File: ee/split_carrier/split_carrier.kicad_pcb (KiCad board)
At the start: 2 copper layers, 127 x 101.6 mm, 11 parts, among them J1 Conn_01x08, J2 Conn_01x08, J3 Conn_01x08, J4 Conn_01x08, J5 Conn_01x04, J6 STM32F0_Discovery_Header, U2 RC1602A

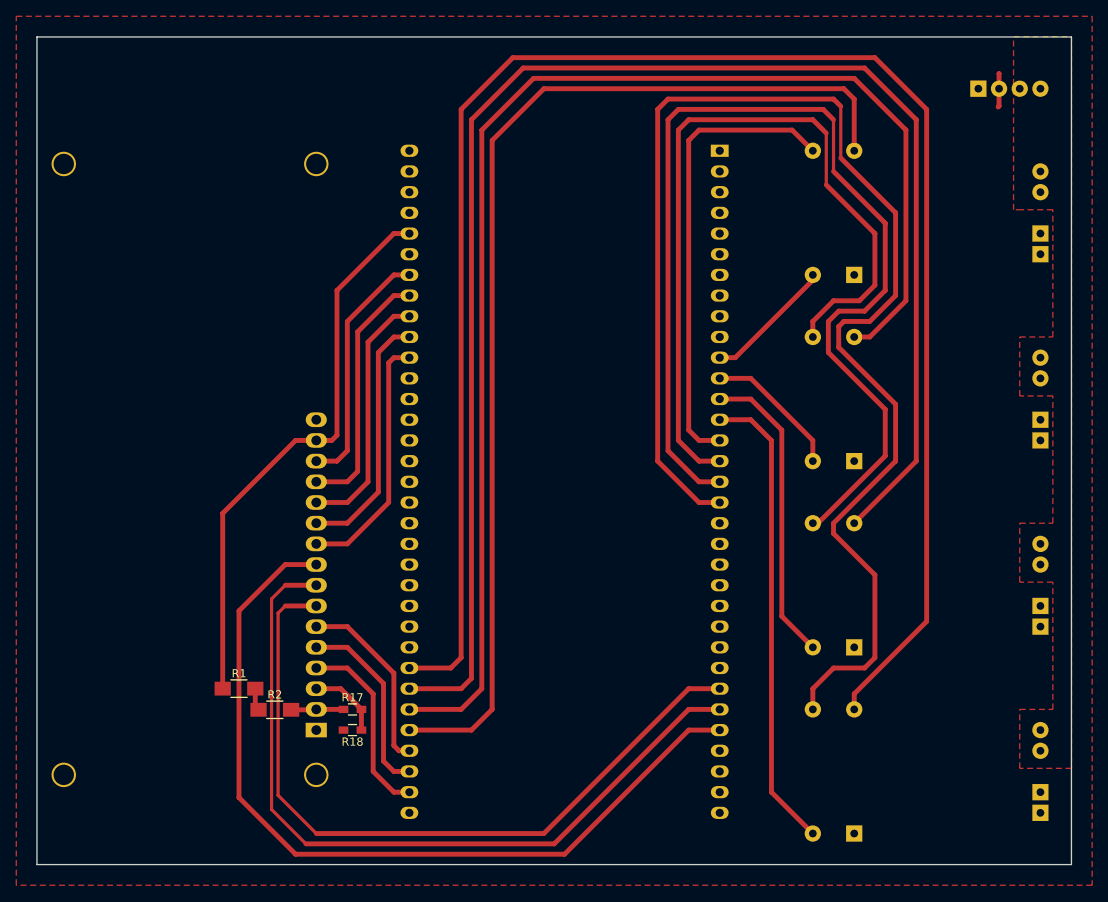
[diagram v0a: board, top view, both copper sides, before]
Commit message: update layout for carrier with new pin assignments
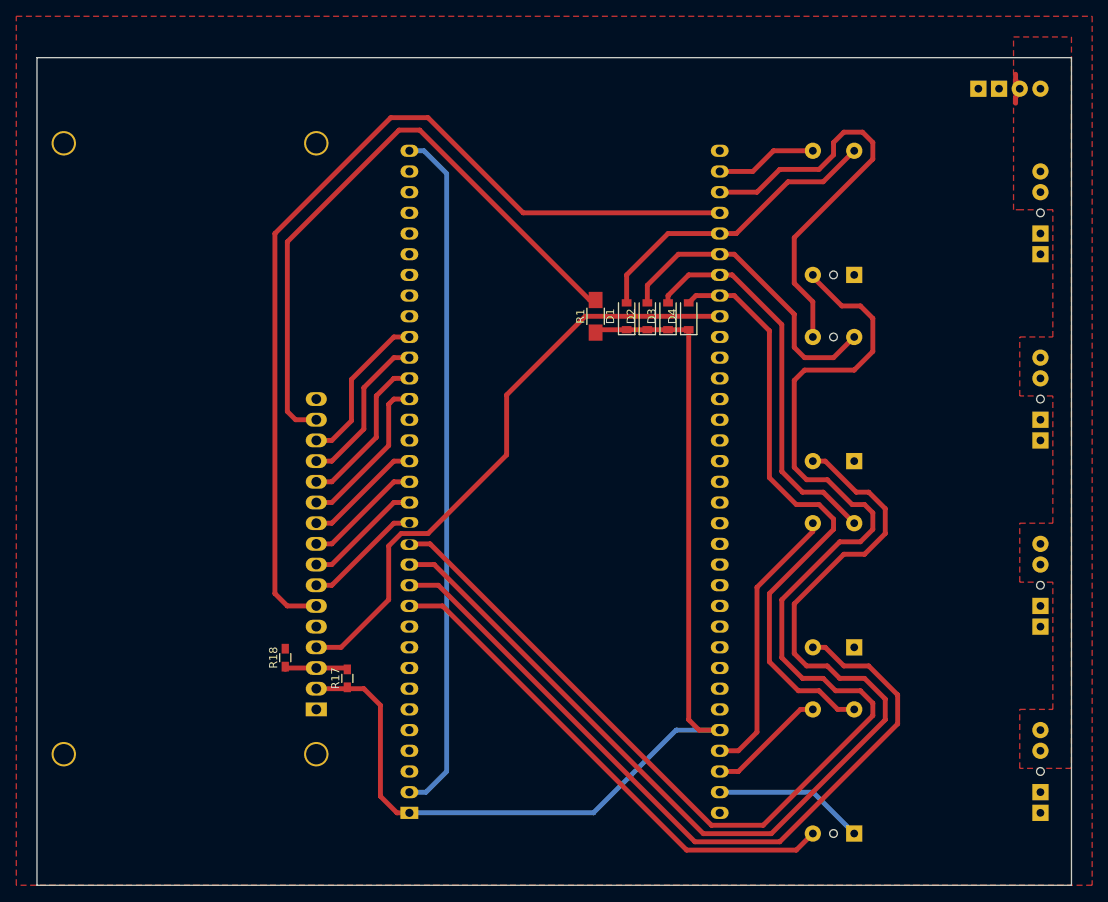
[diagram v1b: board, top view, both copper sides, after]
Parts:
- removed R2: 0, Resistors_SMD:R_1206_HandSoldering
- added D1: D_Schottky, Diodes_SMD:D_SOD-123, F.Cu at (72.4, 34.3)
- added D2: D_Schottky, Diodes_SMD:D_SOD-123, F.Cu at (74.9, 34.3)
- added D3: D_Schottky, Diodes_SMD:D_SOD-123, F.Cu at (77.5, 34.3)
- added D4: D_Schottky, Diodes_SMD:D_SOD-123, F.Cu at (80.0, 34.3)
- J1, J2, J3, J4: footprint custom:Fan_Controller -> custom:Fan_Controller_all
- moved R1 63.3 mm to (68.6, 34.3), turned to 90 degrees
- moved R18 12.1 mm to (30.5, 76.2), turned to 90 degrees
- moved R17 3.86 mm to (38.1, 78.7), turned to 90 degrees
- moved U2 2.54 mm to (34.3, 82.5)
- turned J6 to 270 degrees
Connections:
- net Net-(J6-Pad25) renamed /FAN4_ADC
- net Net-(J6-Pad26) renamed /FAN5_ADC
- net Net-(J6-Pad30) renamed /FAN6_CTRL
- net Net-(J6-Pad31) renamed /FAN7_CTRL
- net Net-(J6-Pad43) renamed /UART1_TX
- net Net-(J6-Pad44) renamed /UART1_RX
- net Net-(J6-Pad47) renamed /SWDIO
- net Net-(J6-Pad50) renamed /SWCLK
- net Net-(J6-Pad51) renamed /FAN4_CTRL
- J6 pad 1: Net-(J6-Pad1) -> +3V3
- J6 pad 11: /FAN0_ADC -> /FAN3_ADC
- J6 pad 12: /FAN1_ADC -> /FAN2_ADC
- J6 pad 13: /FAN2_ADC -> /FAN1_ADC
- J6 pad 14: /FAN3_ADC -> /FAN0_ADC
- J6 pad 15: /FAN0_RPM -> /LCD_D0
- J6 pad 16: /FAN1_RPM -> /LCD_D1
- J6 pad 17: /FAN2_RPM -> /LCD_D2
- J6 pad 18: /FAN3_RPM -> /LCD_D3
- J6 pad 21: Net-(J6-Pad21) -> /LCD_D4
- J6 pad 22: Net-(J6-Pad22) -> /LCD_D5
- J6 pad 23: Net-(J6-Pad23) -> /LCD_D6
- J6 pad 24: Net-(J6-Pad24) -> /LCD_D7
- J6 pad 27: /LCD_D0 -> /FAN6_ADC
- J6 pad 28: /LCD_D1 -> /FAN7_ADC
- J6 pad 29: /LCD_D2 -> Net-(J6-Pad29)
- J6 pad 35: /LCD_RS -> /FAN0_RPM
- J6 pad 36: /LCD_RW -> /FAN1_RPM
- J6 pad 42: Net-(J6-Pad42) -> /LCD_RS
- J6 pad 56: /LCD_D3 -> /FAN5_CTRL
- J6 pad 57: /LCD_D4 -> Net-(J6-Pad57)
- J6 pad 58: /LCD_D5 -> Net-(J6-Pad58)
- J6 pad 59: /LCD_D6 -> Net-(J6-Pad59)
- J6 pad 60: /LCD_D7 -> Net-(J6-Pad60)
- J6 pad 63: Net-(J6-Pad63) -> /FAN2_RPM
- J6 pad 64: Net-(J6-Pad64) -> /FAN3_RPM
- R17 pad 1: Net-(R17-Pad1) -> +3V3
- U2 pad 15: +3V3 -> Net-(R1-Pad2)
- U2 pad 2: Net-(R17-Pad1) -> +3V3
- U2 pad 5: /LCD_RW -> GND
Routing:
- net /FAN3_RPM: track 171.4 -> 14.6 mm
- net /FAN0_ADC: track 16.0 -> 163.9 mm
- net /FAN2_CTRL: track 189.3 -> 48.0 mm
- net /FAN3_CTRL: track 213.9 -> 73.7 mm
- net /FAN1_CTRL: track 165.0 -> 37.8 mm
- net /FAN1_ADC: track 17.1 -> 129.1 mm
- net /FAN2_RPM: track 133.8 -> 34.0 mm
- net GND: track 4.15 -> 103.4 mm
- net /FAN0_CTRL: track 135.0 -> 37.7 mm
- net /LCD_E: track 23.0 -> 115.2 mm
- net /LCD_D2: track 103.0 -> 14.6 mm
- net /LCD_D1: track 95.6 -> 14.6 mm
- net /LCD_D0: track 91.0 -> 14.6 mm
- net Net-(R1-Pad2): track 2.77 -> 77.0 mm
- net +3V3: track 69.1 -> 130.5 mm
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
